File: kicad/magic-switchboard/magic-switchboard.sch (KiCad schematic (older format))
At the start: 26 parts, among them Q1 BC547, Q2 BC547, Q3 BC547, Q4 BC547, SW1 SW_SPST, U1 XY-016

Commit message: unfertige mosfet schaltung
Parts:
- removed D2: Green, switchboard:E10 Edison Socket Print Pins, symbol Device:LED
- removed D3: Blue, switchboard:E10 Edison Socket Print Pins, symbol Device:LED
- removed D4: Yellow, switchboard:E10 Edison Socket Print Pins, symbol Device:LED
- removed Q1, Q2, Q3, Q4: BC547, Package_TO_SOT_THT:TO-92_Inline, symbol Transistor_BJT:BC547
- removed R5, R6, R7, R8: 10k, Resistor_THT:R_Axial_DIN0414_L11.9mm_D4.5mm_P15.24mm_Horizontal, symbol Device:R
- removed SW1: SW_SPST, digikey-footprints:Switch_Toggle_ATE1D-2M3-10-Z, symbol Switch:SW_SPST
- added D? (x3): Red, switchboard:E10 Edison Socket Print Pins, symbol Device:LED
- added Q? (x5): 2N7000, digikey-footprints:TO-92-3, symbol dk_Transistors-FETs-MOSFETs-Single:2N7000
- added Q?: BS250, Package_TO_SOT_THT:TO-92_Inline, symbol Transistor_FET:BS250
- added R?: 10k, Resistor_THT:R_Axial_DIN0414_L11.9mm_D4.5mm_P15.24mm_Horizontal, symbol Device:R
- added S?: MTS-203, digikey-footprints:Switch_Slide_JS202011SCQN, symbol dk_Slide-Switches:JS202011SCQN
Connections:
- wire segments 66 -> 76
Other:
- moved on the sheet: A1, BT1, C1, C2, D1, R1, R2, R3, R4, U1

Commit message: p-channel deadman trap
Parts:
- removed Q?: 2N7000, digikey-footprints:TO-92-3, symbol dk_Transistors-FETs-MOSFETs-Single:2N7000
- removed R1, R2, R3, R4: 10k, Resistor_THT:R_Axial_DIN0414_L11.9mm_D4.5mm_P15.24mm_Horizontal, symbol Device:R
- removed S1, S2, S3, S4: ATE1D-2M3-10-Z, digikey-footprints:Switch_Toggle_ATE1D-2M3-10-Z, symbol dk_Toggle-Switches:ATE1D-2M3-10-Z
- added Q?: BC547, Package_TO_SOT_THT:TO-92_Inline, symbol Transistor_BJT:BC547
- added R?: 10k, Resistor_THT:R_Axial_DIN0414_L11.9mm_D4.5mm_P15.24mm_Horizontal, symbol Device:R
- added S? (x3): MTS-203, digikey-footprints:Switch_Slide_JS202011SCQN, symbol dk_Slide-Switches:JS202011SCQN
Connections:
- net labels added: deadmantrap, powerswitch
- wire segments 76 -> 87
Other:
- moved on the sheet: D1, D?, Q?, S?

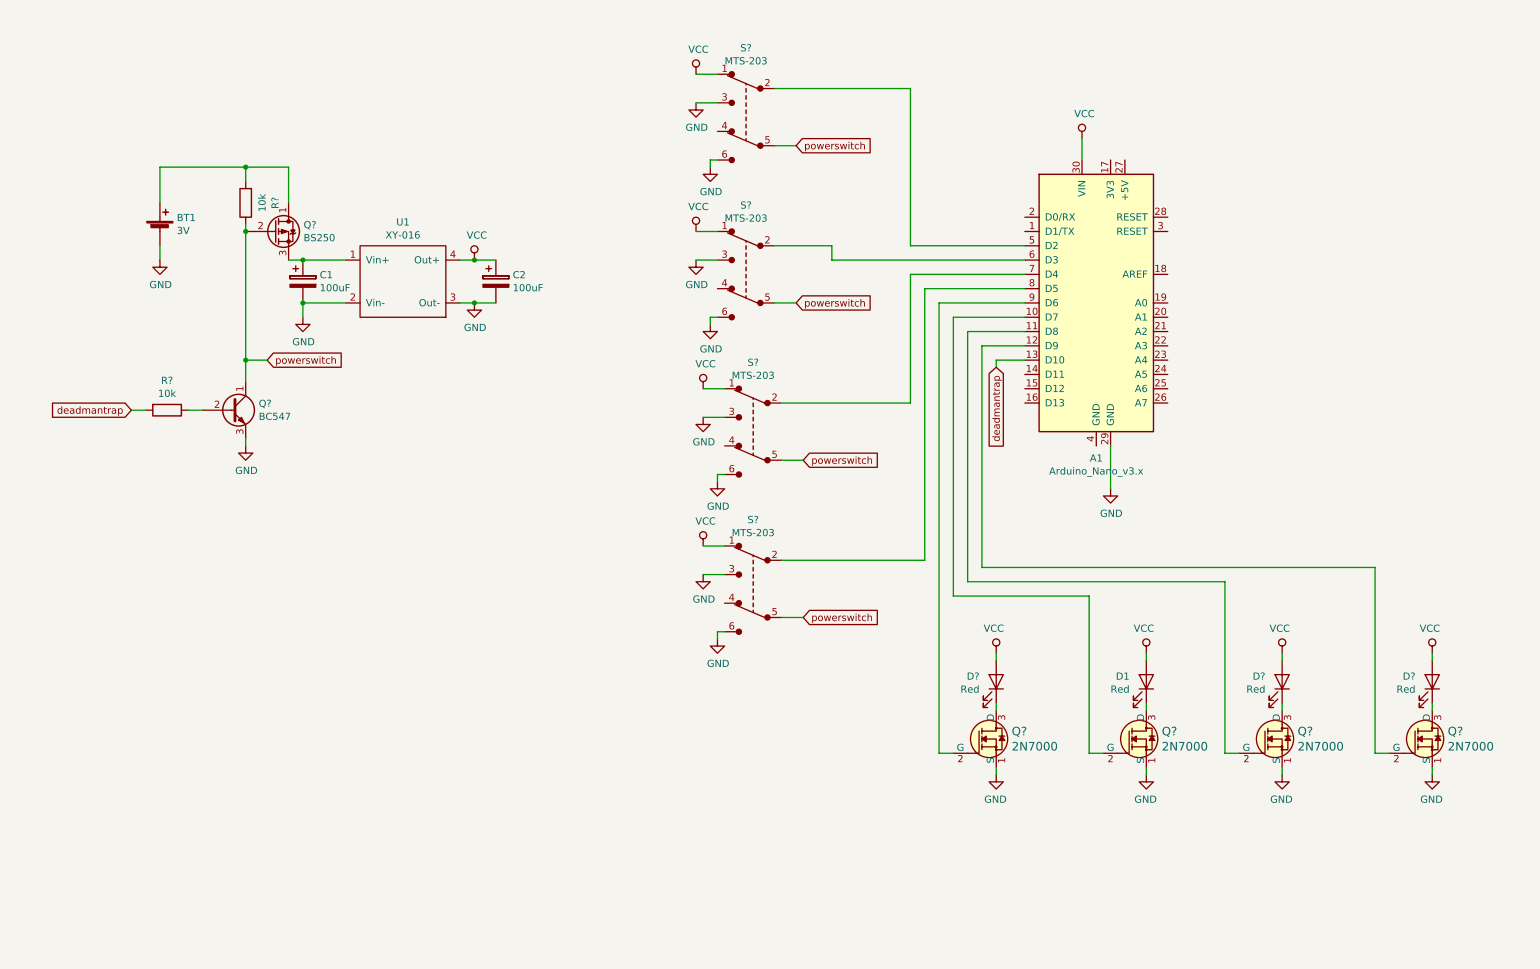
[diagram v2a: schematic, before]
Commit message: redone pcb v3
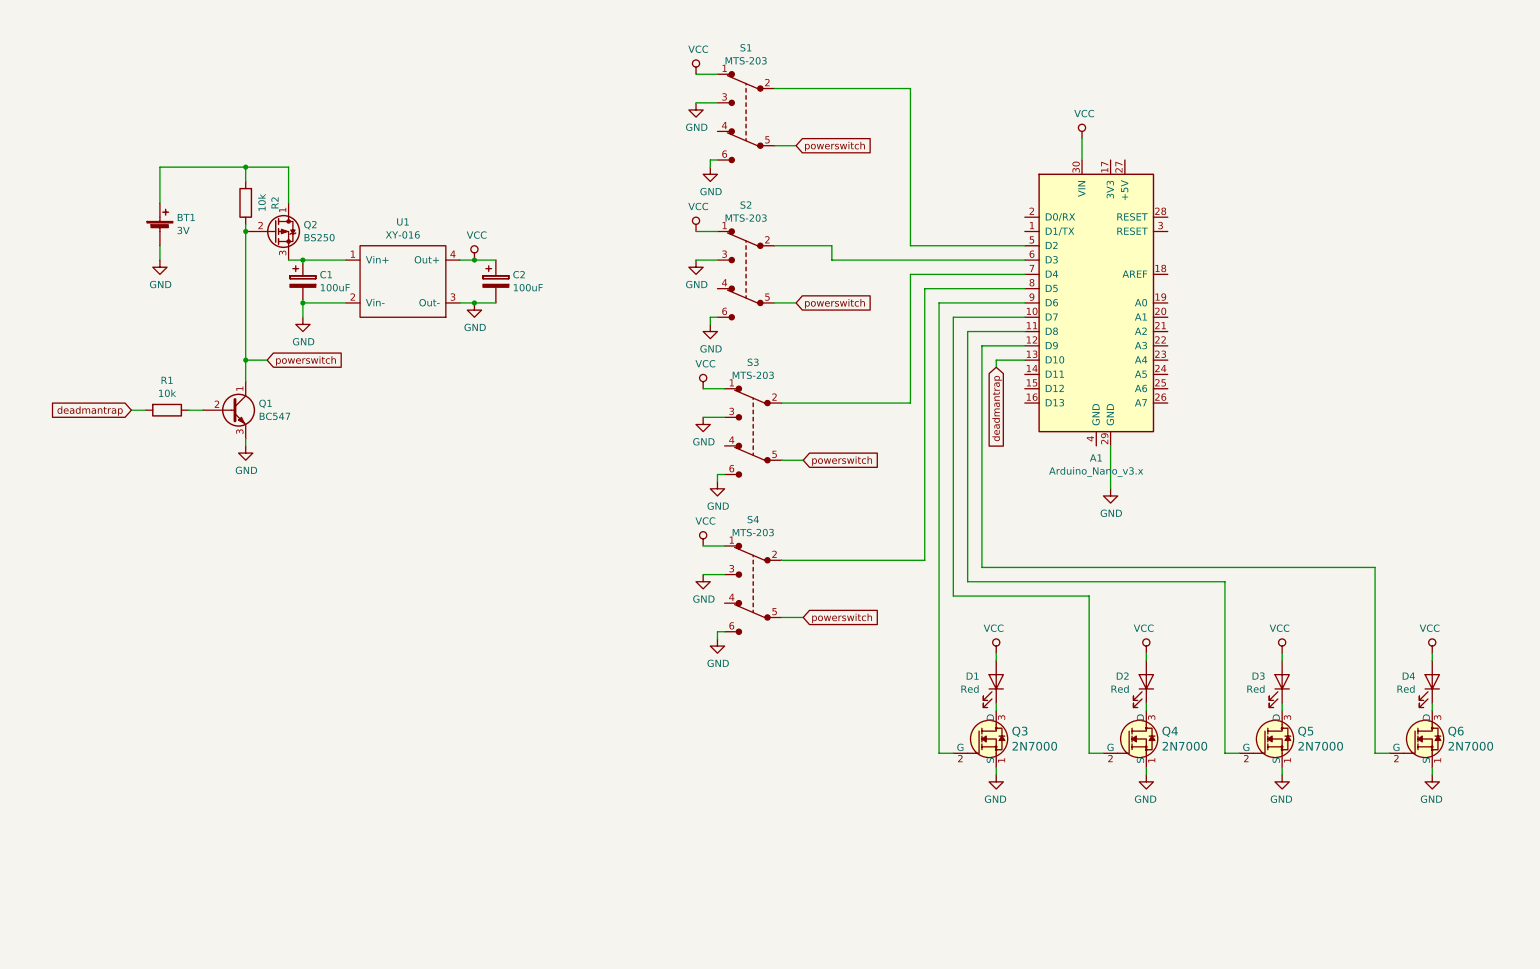
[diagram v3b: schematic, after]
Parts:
- A1: footprint Module:Arduino_Nano -> switchboard:Arduino_Nano
- BT1: footprint Battery:BatteryHolder_Keystone_3009_1x2450 -> switchboard:BatteryHolder_Keystone_3009_1x2450
- C1, C2: footprint Capacitor_THT:CP_Radial_D6.3mm_P2.50mm -> switchboard:CP_Radial_D6.3mm_P2.50mm
- Q1: renamed from Q?; footprint Package_TO_SOT_THT:TO-92_Inline -> switchboard:BC547
- Q2: renamed from Q?; footprint Package_TO_SOT_THT:TO-92_Inline -> switchboard:BS250
- Q3, Q4, Q5, Q6: renamed from Q?; footprint digikey-footprints:TO-92-3 -> switchboard:2N700
- R1, R2: renamed from R?; footprint Resistor_THT:R_Axial_DIN0414_L11.9mm_D4.5mm_P15.24mm_Horizontal -> switchboard:Resistor
- S1, S2, S3, S4: renamed from S?; footprint digikey-footprints:Switch_Slide_JS202011SCQN -> switchboard:MTS-203 Switch
- gave numbers to parts that had none: 3
- renumbered D1 to D2

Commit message: created gerbers for v3
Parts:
- added U2: alternative Boost Converter, switchboard:BoostConverter3Pin, symbol switchboard:BoostConverter
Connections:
- net GND: now also U2.2 (GND)
- net VCC: now also U2.3 (Vout)
- net at C1.1, Q2.3 (S), U1.1 (Vin+): now also U2.1 (Vin)
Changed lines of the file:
@@
 U 1 1 5C2A4AF6
 P 3400 2400
-F 0 "U1" H 3400 2815 50  0000 C CNN
+F 0 "U1" H 3400 2400 50  0000 C CNN
 F 1 "XY-016" H 3400 2724 50  0000 C CNN
 F 2 "switchboard:XY-016" H 3400 2500 50  0001 C CNN
@@
 	3000 2550 2700 2550
 Wire Wire Line
-	2700 2250 3000 2250
+	2700 2250 2950 2250
 $Comp
 L power:GND #PWR023
@@
 Wire Wire Line
 	6050 4350 7050 4350
+$Comp
+L switchboard:BoostConverter U2
+U 1 1 5C4DCF30
+P 3400 1400
+F 0 "U2" H 3400 1665 50  0000 C CNN
+F 1 "alternative Boost Converter" H 3400 1574 50  0000 C CNN
+F 2 "switchboard:BoostConverter3Pin" H 3400 1400 50  0001 C CNN
+F 3 "" H 3400 1400 50  0001 C CNN
+	1    3400 1400
+	1    0    0    -1
+$EndComp
+Connection ~ 2950 2250
+Wire Wire Line
+	2950 2250 3000 2250
+Connection ~ 4050 2250
+$Comp
+L power:GND #PWR028
+U 1 1 5C4E17B4
+P 3400 1750
+F 0 "#PWR028" H 3400 1500 50  0001 C CNN
+F 1 "GND" H 3405 1577 50  0000 C CNN
+F 2 "" H 3400 1750 50  0001 C CNN
+F 3 "" H 3400 1750 50  0001 C CNN
+	1    3400 1750
+	1    0    0    -1
+$EndComp
+Wire Wire Line
+	3100 1400 2950 1400
+Wire Wire Line
+	2950 1400 2950 2250
+Wire Wire Line
+	3700 1400 4050 1400
+Wire Wire Line
+	4050 1400 4050 2250
 $EndSCHEMATC

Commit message: attiny2313 board
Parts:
- removed A1: Arduino_Nano_v3.x, switchboard:Arduino_Nano, symbol MCU_Module:Arduino_Nano_v3.x
- removed Q2: BS250, switchboard:BS250, symbol Transistor_FET:BS250
- removed Q3, Q4, Q5, Q6: 2N7000, switchboard:2N700, symbol dk_Transistors-FETs-MOSFETs-Single:2N7000
- removed S1, S2, S3, S4: MTS-203, switchboard:MTS-203 Switch, symbol dk_Slide-Switches:JS202011SCQN
- removed U1: XY-016, switchboard:XY-016, symbol switchboard:XY-016
- added J1: AVR-ISP-6, switchboard:ISP6, symbol Connector:AVR-ISP-6
- added Q2, Q3, Q4: BC547, Package_TO_SOT_THT:TO-92_Inline, symbol Transistor_BJT:BC547
- added R3, R4: 10k, switchboard:Resistor, symbol Device:R
- added SW1, SW2, SW3, SW4: MTS-103, switchboard:MTS-103 Switch, symbol switchboard:MTS-103
- added U1: ATtiny2313A-PU, switchboard:ATtiny2313, symbol switchboard:ATtiny2313A-PU
- Q1: footprint switchboard:BC547 -> Package_TO_SOT_THT:TO-92_Inline
- U2: value alternative Boost Converter -> 5V Boost
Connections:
- net GND: now also J1.6 (GND), Q2.3 (E), Q3.3 (E), Q4.3 (E), SW1.3 (Off), SW2.3 (Off), SW3.3 (Off), SW4.3 (Off), U1.10 (GND)
- net VCC: now also BT1.1 (+), C1.1, U2.1 (Vin), J1.2 (VCC), SW1.1 (ON), SW2.1 (ON), SW3.1 (ON), SW4.1 (ON), U1.20 (VCC); no longer C2.1, D1.2 (A), D2.2 (A), D3.2 (A), D4.2 (A), U2.3 (Vout)
- net at R2.2: now also J1.4 (MOSI), U1.17 (PB5); no longer BT1.1 (+)
- net at D2.1 (K): now also Q2.1 (C)
- net at D1.1 (K): now also Q1.1 (C)
- net at D4.1 (K): now also Q4.1 (C)
- net at D3.1 (K): now also Q3.1 (C)
- net deadmantrap: no longer names the net of R1.2
- net deadmantrap: now also U1.16 (PB4)
- net powerswitch: no longer names the net of R2.1
- net powerswitch: now also Q2.2 (B); no longer Q1.1 (C)
- new net: SW1.2 (Out), U1.12 (PB0)
- new net: J1.5 (~RST), U1.1 (PA2/~RESET)
- new net: SW2.2 (Out), U1.13 (PB1)
- new net: SW3.2 (Out), U1.14 (PB2)
- new net: SW4.2 (Out), U1.15 (PB3)
- new net: J1.1 (MISO), R3.2, U1.18 (PB6)
- new net: J1.3 (SCK), R4.2, U1.19 (PB7)
- new net: Q3.2 (B), R3.1
- new net: Q4.2 (B), R4.1
- new net +5V: C2.1, D1.2 (A), D2.2 (A), D3.2 (A), D4.2 (A), U2.3 (Vout)
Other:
- moved on the sheet: BT1, C1, C2, D1, D2, D3, U2
